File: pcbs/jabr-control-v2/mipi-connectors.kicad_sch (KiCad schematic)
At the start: 5 parts, among them J1501 FH12-22S-0.5SH, J1502 FH12-22S-0.5SH

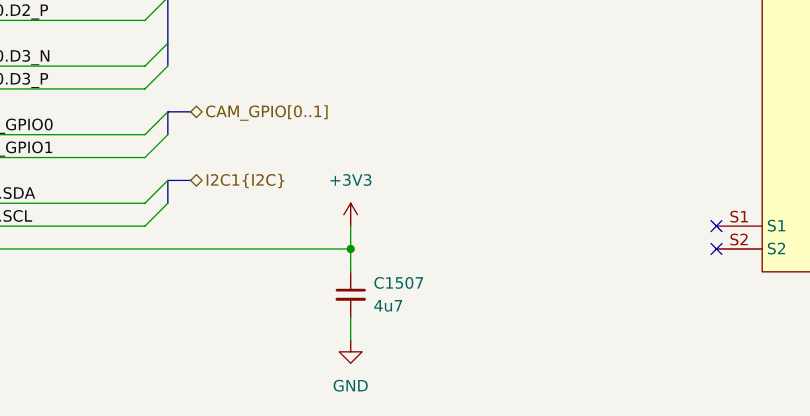
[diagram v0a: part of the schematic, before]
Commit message: PCI11010C Schematic sheet mostly done
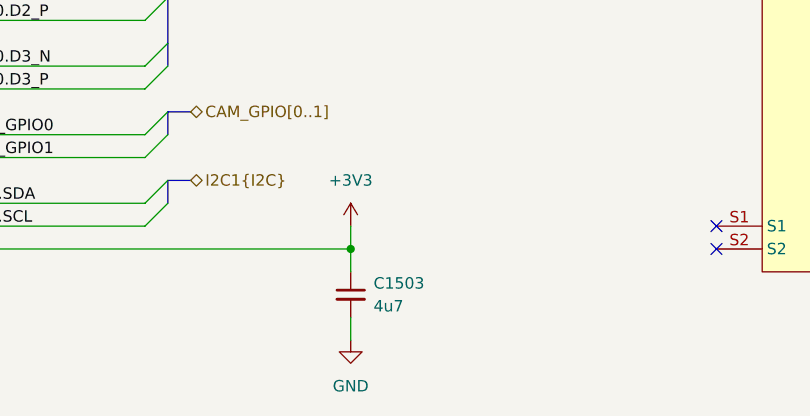
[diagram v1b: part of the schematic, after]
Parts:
- renumbered C1507 to C1503

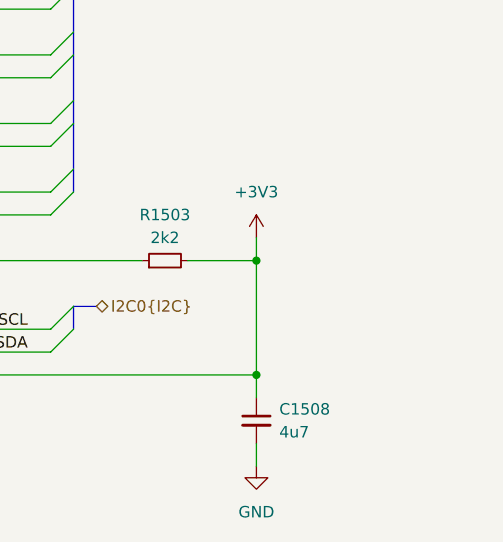
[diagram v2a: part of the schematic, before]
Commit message: PCI11010 IO done
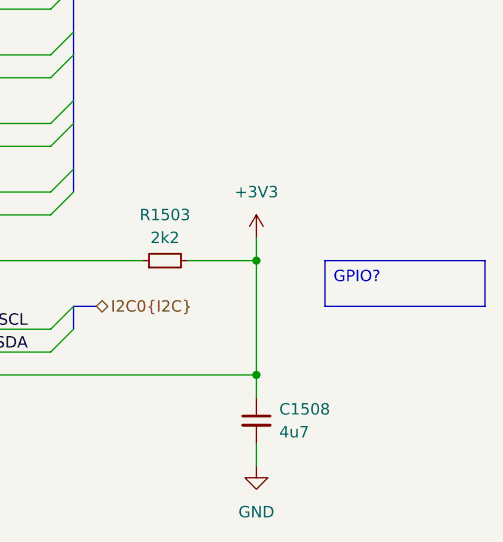
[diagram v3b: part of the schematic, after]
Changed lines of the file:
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@@
+		)
+	)
+	(text_box "GPIO?"
+		(exclude_from_sim no)
+		(at 248.92 111.76 0)
+		(size 17.78 5.08)
+		(margins 0.9525 0.9525 0.9525 0.9525)
+		(stroke
+			(width 0)
+			(type solid)
+			(color 255 0 0 1)
+		)
+		(fill
+			(type none)
+		)
+		(effects
+			(font
+				(size 1.27 1.27)
+				(color 255 0 0 1)
+			)
+			(justify left top)
 		)
 	)

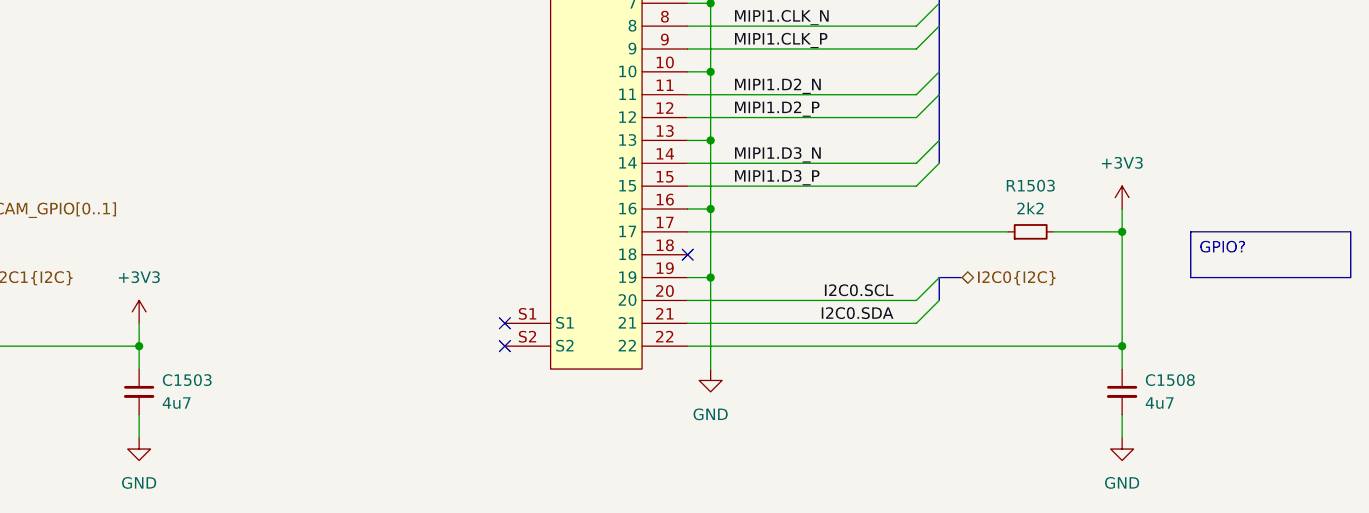
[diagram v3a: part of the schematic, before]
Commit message: Removed power button reset to switch (power will be cycled anyway)
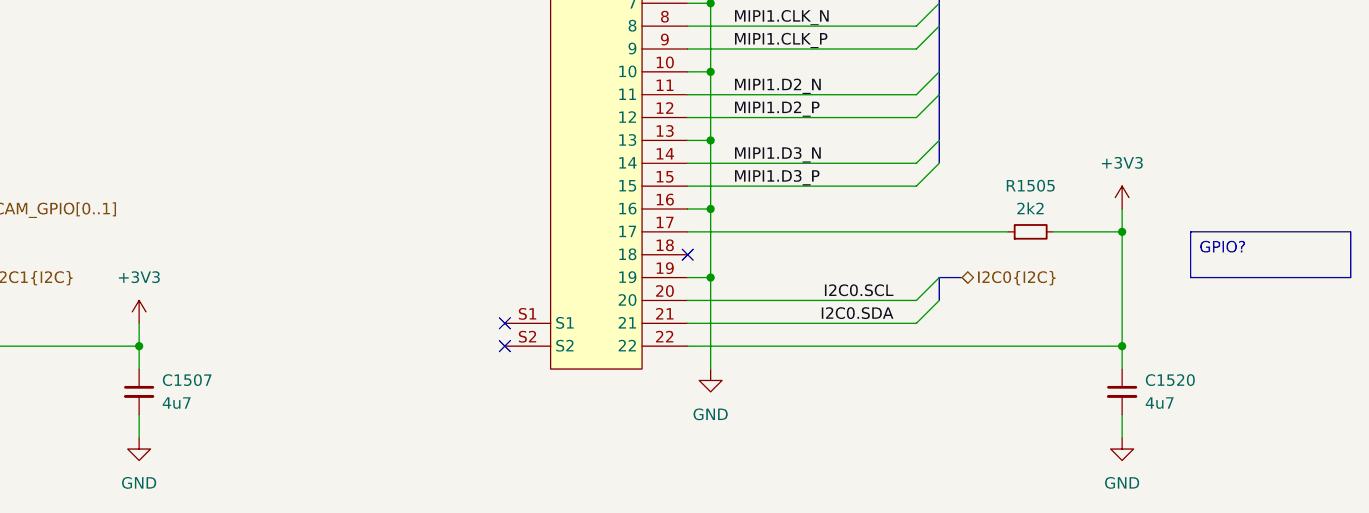
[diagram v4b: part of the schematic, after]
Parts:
- renumbered C1503 to C1507, C1508 to C1520, R1503 to R1505
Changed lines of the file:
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@@
 		(dnp no)
 		(fields_autoplaced yes)
-		(property "Reference" "#PWR01505"
+		(property "Reference" "#PWR01512"
 			(at 132.08 125.73 0)
 			(hide yes)
@@
 			(project "jabr-control-v2"
 				(path "/f91ec272-d09a-4038-bbbb-962739a92c51/80b60915-5ccb-4842-b09a-a259b4f355b7"
-					(reference "#PWR01505")
+					(reference "#PWR01512")
 					(unit 1)
 				)
@@
 		(dnp no)
 		(fields_autoplaced yes)
-		(property "Reference" "R1503"
+		(property "Reference" "R1505"
 			(at 231.14 106.68 90)
 			(show_name no)
@@
 			(project "jabr-control-v2"
 				(path "/f91ec272-d09a-4038-bbbb-962739a92c51/80b60915-5ccb-4842-b09a-a259b4f355b7"
-					(reference "R1503")
+					(reference "R1505")
 					(unit 1)
 				)
@@
 		(dnp no)
 		(fields_autoplaced yes)
-		(property "Reference" "C1503"
+		(property "Reference" "C1507"
 			(at 134.62 128.2762 0)
 			(show_name no)
@@
 			(project "jabr-control-v2"
 				(path "/f91ec272-d09a-4038-bbbb-962739a92c51/80b60915-5ccb-4842-b09a-a259b4f355b7"
-					(reference "C1503")
+					(reference "C1507")
 					(unit 1)
 				)
@@
 		(dnp no)
 		(fields_autoplaced yes)
-		(property "Reference" "#PWR01506"
+		(property "Reference" "#PWR01513"
 			(at 132.08 140.97 0)
 			(hide yes)
@@
 			(project "jabr-control-v2"
 				(path "/f91ec272-d09a-4038-bbbb-962739a92c51/80b60915-5ccb-4842-b09a-a259b4f355b7"
-					(reference "#PWR01506")
+					(reference "#PWR01513")
 					(unit 1)
 				)
@@
 		(dnp no)
 		(fields_autoplaced yes)
-		(property "Reference" "C1508"
+		(property "Reference" "C1520"
 			(at 243.84 128.2762 0)
 			(show_name no)
@@
 			(project "jabr-control-v2"
 				(path "/f91ec272-d09a-4038-bbbb-962739a92c51/80b60915-5ccb-4842-b09a-a259b4f355b7"
-					(reference "C1508")
+					(reference "C1520")
 					(unit 1)
 				)
@@
 		(dnp no)
 		(fields_autoplaced yes)
-		(property "Reference" "#PWR01512"
+		(property "Reference" "#PWR01521"
 			(at 241.3 113.03 0)
 			(hide yes)
@@
 			(project "jabr-control-v2"
 				(path "/f91ec272-d09a-4038-bbbb-962739a92c51/80b60915-5ccb-4842-b09a-a259b4f355b7"
-					(reference "#PWR01512")
+					(reference "#PWR01521")
 					(unit 1)
 				)
@@
 		(dnp no)
 		(fields_autoplaced yes)
-		(property "Reference" "#PWR01503"
+		(property "Reference" "#PWR01505"
 			(at 86.36 133.35 0)
 			(hide yes)
@@
 			(project "jabr-control-v2"
 				(path "/f91ec272-d09a-4038-bbbb-962739a92c51/80b60915-5ccb-4842-b09a-a259b4f355b7"
-					(reference "#PWR01503")
+					(reference "#PWR01505")
 					(unit 1)
 				)
@@
 		(dnp no)
 		(fields_autoplaced yes)
-		(property "Reference" "#PWR01509"
+		(property "Reference" "#PWR01518"
 			(at 195.58 133.35 0)
 			(hide yes)
@@
 			(project "jabr-control-v2"
 				(path "/f91ec272-d09a-4038-bbbb-962739a92c51/80b60915-5ccb-4842-b09a-a259b4f355b7"
-					(reference "#PWR01509")
+					(reference "#PWR01518")
 					(unit 1)
 				)
@@
 		(dnp no)
 		(fields_autoplaced yes)
-		(property "Reference" "#PWR01513"
+		(property "Reference" "#PWR01522"
 			(at 241.3 140.97 0)
 			(hide yes)
@@
 			(project "jabr-control-v2"
 				(path "/f91ec272-d09a-4038-bbbb-962739a92c51/80b60915-5ccb-4842-b09a-a259b4f355b7"
-					(reference "#PWR01513")
+					(reference "#PWR01522")
 					(unit 1)
 				)

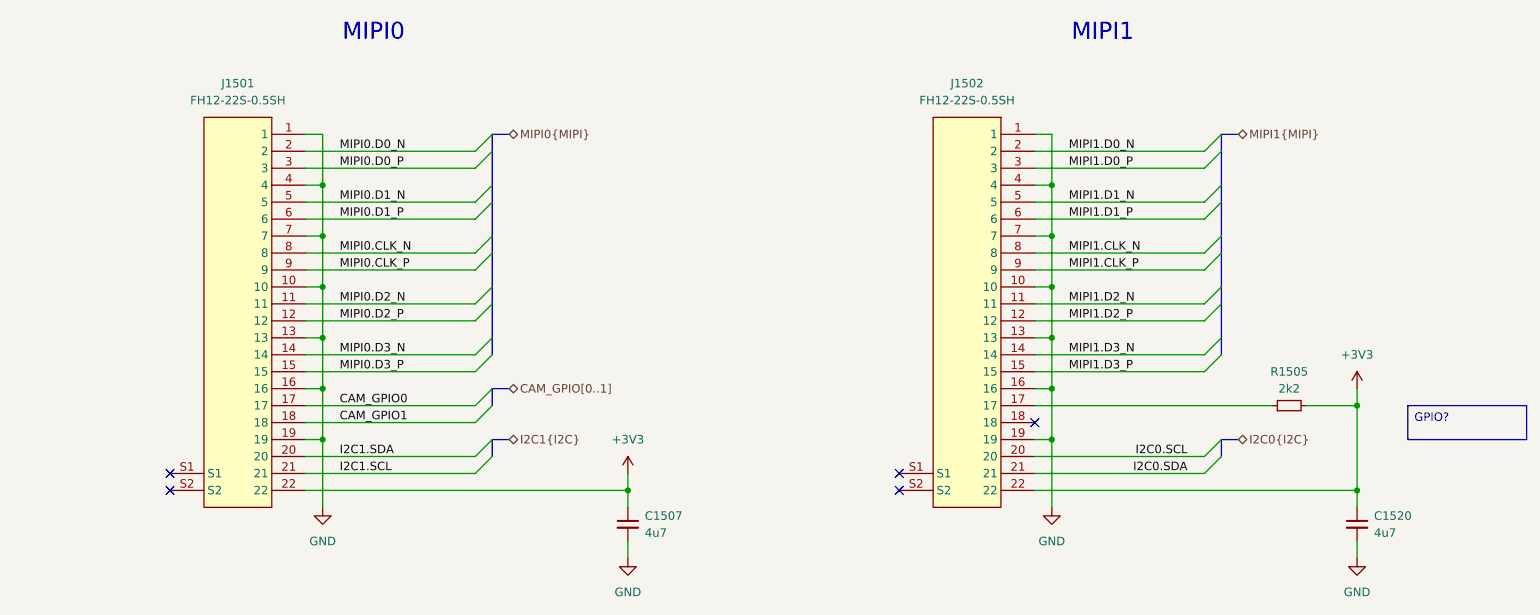
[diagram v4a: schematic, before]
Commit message: Schematic done
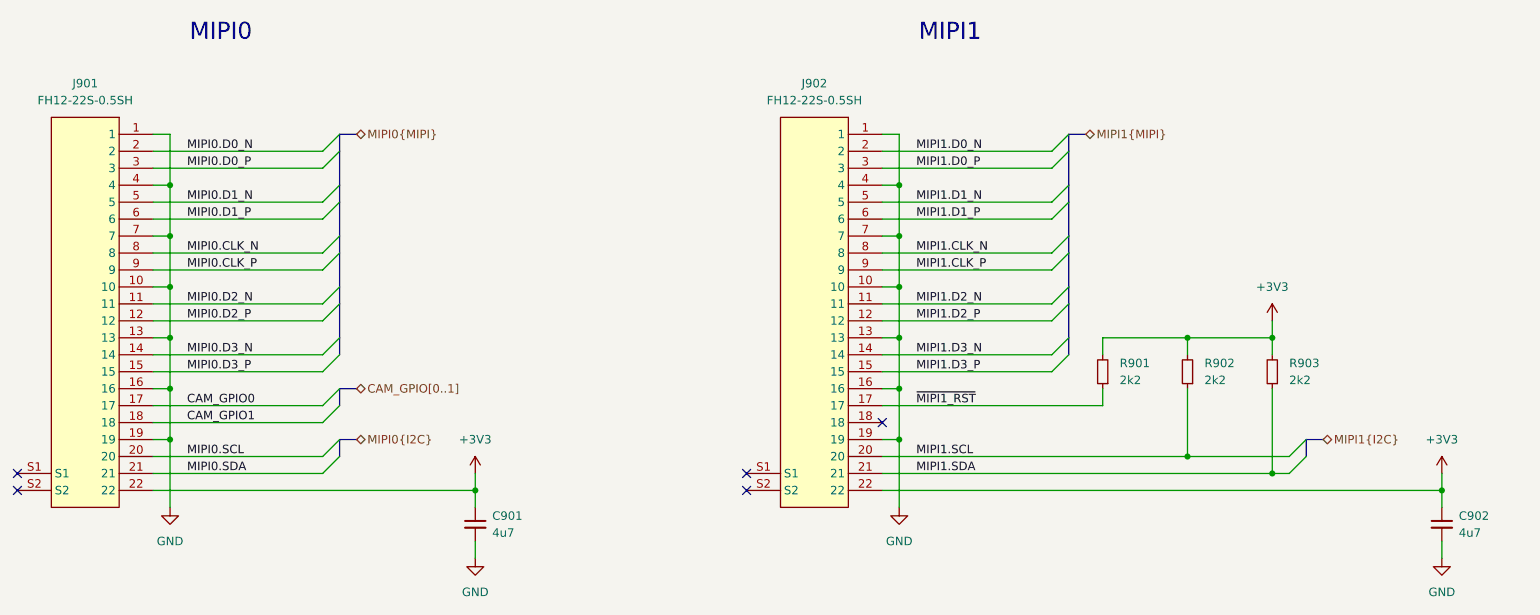
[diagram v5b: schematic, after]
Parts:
- removed R1505: 2k2, symbol DEV:R_SMALL
- added R901, R902, R903: 2k2, project_footprints:R_0402, symbol DEV:R_SMALL
- renumbered C1507 to C901, C1520 to C902, J1501 to J901, J1502 to J902
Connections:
- net +3V3: now also R901.2, R902.2, R903.2
- net ~{MIPI1_RST}: now reaches J902.17
- net ~{MIPI1_RST}: now also R901.1
- net I2C0.SCL renamed MIPI1.SCL
- net MIPI1.SCL: now also R902.1
- net I2C0.SDA renamed MIPI1.SDA
- net MIPI1.SDA: now also R903.1
- net I2C1.SCL renamed MIPI0.SDA
- net I2C1.SDA renamed MIPI0.SCL
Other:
- moved on the sheet: C901, C902, J901, J902
